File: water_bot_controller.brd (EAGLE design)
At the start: 100 x 80 mm, 55 parts

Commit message: added microcontroller module, cleaned up relay driver module
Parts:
- removed LED2, LED3, LED4: (no value), led:SMARTLED-TTW
- removed R10, R11, R12: 10k, rcl:R0603
- removed R7, R8, R9: 0 ohm, rcl:R0603
- added C1: 1uF, rcl:C0603
- added C2, C6: 0.1uF, rcl:C0603
- added C3, C5: 4.7uF, rcl:C1206
- added C4: 10uF, rcl:C1206
- added D1: MMBD4148DICT, LEDdynamics:SOT23
- added R22, R23: 10K, rcl:R0603
- added R24: 10 ohm, rcl:R0603
- added U$1: PSOC_4000, stovelite:SOIC16
- added U2: LM3480IM3-5.0, LEDdynamics:SOT-23
- IC1: value (none) -> ULN2803A
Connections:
- removed net 6C: IC1.13
- removed net 7C: IC1.12
- removed net 8C: IC1.11
- removed net N$10: IC1.7, R8.2
- removed net N$11: IC1.8, R9.2
- removed net N$12: IC1.2, R3.2
- removed net N$18: LED4.A@1, R12.1
- removed net N$19: LED3.A@1, R11.1
- removed net N$20: LED2.A@1, R10.1
- removed net N$9 (its old number): IC1.6, R7.2
- removed net P6: R12.2, R7.1
- removed net P7: R11.2, R8.1
- removed net P8: R10.2, R9.1
- new net N$37: C1.2, U$1.6
- new net N$38: D1.3, R24.1
- new net N$39: C4.1, R24.2, U2.2
- new net N$6: R3.2
- new net P0.2: R22.1, R23.2, U$1.4
- new net SCLK: U$1.2
- new net SDAT: U$1.1
- new net VDD: C2.1, C3.1, C5.1, C6.1, R22.2, U$1.7, U2.3
- net +12V: now also D1.1
- net GND: now also C1.1, C2.2, C3.2, C4.2, C5.2, C6.2, LED13.C@1, R23.1, U$1.8, U2.1; no longer LED2.C@1, LED3.C@1, LED4.C@1
- net N$35: now also R21.2
- net P1: now also U$1.16
- net P2: now also U$1.15
- net P3: now also U$1.14
- net P4: now also U$1.13
- net P5: now also U$1.12

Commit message: cleaned up relay module
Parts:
- removed LED11, LED12, LED13: (no value), led:SMARTLED-TTW
- removed R18, R19, R20, R21: 10K, rcl:R0603
- added LED2, LED3, LED4: (no value), led:SMARTLED-TTW
- added R10, R7, R8, R9: 10K, rcl:R0603
- moved LED10 519.6 mm to (-48.3, -709.9)
- moved RELAY_4 382.5 mm to (-73.7, -626.1)
- moved F4 354.5 mm to (-71.1, -647.7)
- moved F5 354.5 mm to (-71.1, -717.5)
- moved RELAY_5 354.5 mm to (-73.7, -696.0)
- moved TP7 354.5 mm to (-86.4, -664.2)
- moved TP8 354.5 mm to (-77.5, -664.2)
- moved TP10 354.5 mm to (-77.5, -734.1)
- moved TP9 354.5 mm to (-86.4, -734.1)
- moved TP5 315.6 mm to (-86.4, -594.4)
- moved TP6 315.6 mm to (-77.5, -594.4)
- moved F2 310.1 mm to (-71.1, -508.0)
- moved F3 310.1 mm to (-71.1, -577.9)
- moved RELAY_2 310.0 mm to (-73.7, -486.4)
- moved RELAY_3 310.0 mm to (-73.7, -556.3)
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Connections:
- net N$3 renamed R1
- removed net N$1 (its old number): RELAY_1.5, TP1.TP
- removed net N$21: RELAY_2.5, TP3.TP
- removed net N$23: F2.2, R18.2, TP4.TP
- removed net N$24: LED10.A@1, R18.1
- removed net N$25: RELAY_3.5, TP5.TP
- removed net N$27: F3.2, R19.2, TP6.TP
- removed net N$28: LED11.A@1, R19.1
- removed net N$29: RELAY_4.5, TP7.TP
- removed net N$31: F4.2, R20.2, TP8.TP
- removed net N$32: LED12.A@1, R20.1
- removed net N$33: RELAY_5.5, TP9.TP
- removed net N$35: F5.2, R21.2, TP10.TP
- removed net N$36: LED13.A@1, R21.1
- new net N$11: LED3.A@1, R8.1
- new net N$18: LED4.A@1, R9.1
- new net N$20: LED10.A@1, R10.1
- new net N$4: LED2.A@1, R7.1
- new net R2: F2.2, R7.2, TP4.TP
- new net R3: F3.2, R8.2, TP6.TP
- new net R4: F4.2, R9.2, TP8.TP
- new net R5: F5.2, R10.2, TP10.TP
- net 1C: now also RELAY_1.5, TP1.TP
- net 2C: now also RELAY_2.5, TP3.TP
- net 3C: now also RELAY_3.5, TP5.TP
- net 4C: now also RELAY_4.5, TP7.TP
- net 5C: now also RELAY_5.5, TP9.TP
- net GND: now also LED2.C@1, LED3.C@1, LED4.C@1; no longer LED11.C@1, LED12.C@1, LED13.C@1

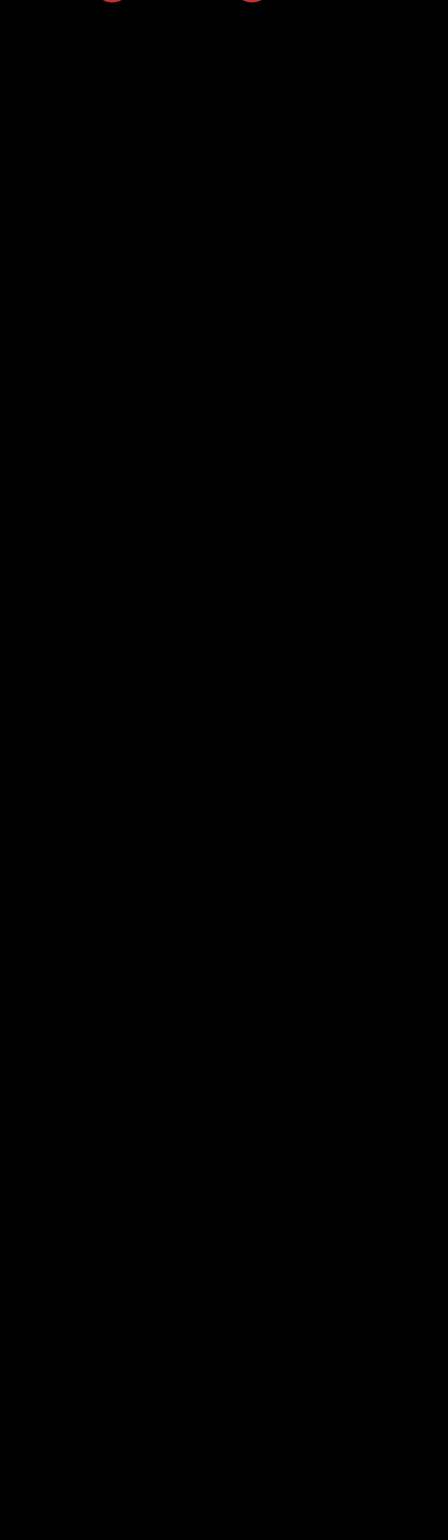
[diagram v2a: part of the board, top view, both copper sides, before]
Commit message: spec'd pwr/sig conns, added pushbuttons to schematic
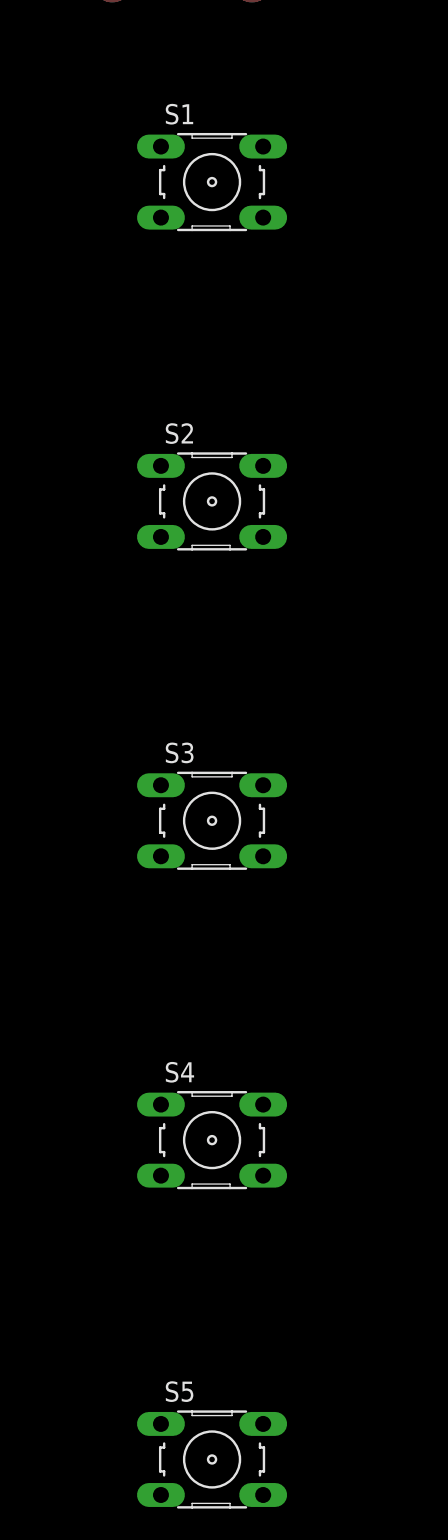
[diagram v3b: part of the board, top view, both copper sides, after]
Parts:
- added S1, S2, S3, S4, S5: (no value), switch-omron:B3F-10XX
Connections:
- net P1: now also S1.4
- net P2: now also S2.4
- net P3: now also S3.4
- net P4: now also S4.4
- net P5: now also S5.4
- net VDD: now also S1.2, S2.2, S3.2, S4.2, S5.2
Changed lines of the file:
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@@
 <element name="R10" library="rcl" library_urn="urn:adsk.eagle:library:334" package="R0603" package3d_urn="urn:adsk.eagle:package:23555/2" value="10K" x="-71.12" y="-732.79"/>
 <element name="LED10" library="led" library_urn="urn:adsk.eagle:library:259" package="SMARTLED-TTW" package3d_urn="urn:adsk.eagle:package:15825/1" value="" x="-48.26" y="-709.93"/>
+<element name="S1" library="switch-omron" library_urn="urn:adsk.eagle:library:377" package="B3F-10XX" package3d_urn="urn:adsk.eagle:package:27496/1" value="" x="-80.01" y="-746.76">
+<attribute name="MF" value="" x="-80.01" y="-746.76" size="1.778" layer="27" display="off"/>
+<attribute name="MPN" value="B3F-1000" x="-80.01" y="-746.76" size="1.778" layer="27" display="off"/>
+<attribute name="OC_FARNELL" value="176432" x="-80.01" y="-746.76" size="1.778" layer="27" display="off"/>
+<attribute name="OC_NEWARK" value="36M3542" x="-80.01" y="-746.76" size="1.778" layer="27" display="off"/>
+</element>
+<element name="S2" library="switch-omron" library_urn="urn:adsk.eagle:library:377" package="B3F-10XX" package3d_urn="urn:adsk.eagle:package:27496/1" value="" x="-80.01" y="-767.08">
+<attribute name="MF" value="" x="-80.01" y="-767.08" size="1.778" layer="27" display="off"/>
+<attribute name="MPN" value="B3F-1000" x="-80.01" y="-767.08" size="1.778" layer="27" display="off"/>
+<attribute name="OC_FARNELL" value="176432" x="-80.01" y="-767.08" size="1.778" layer="27" display="off"/>
+<attribute name="OC_NEWARK" value="36M3542" x="-80.01" y="-767.08" size="1.778" layer="27" display="off"/>
+</element>
+<element name="S3" library="switch-omron" library_urn="urn:adsk.eagle:library:377" package="B3F-10XX" package3d_urn="urn:adsk.eagle:package:27496/1" value="" x="-80.01" y="-787.4">
+<attribute name="MF" value="" x="-80.01" y="-787.4" size="1.778" layer="27" display="off"/>
+<attribute name="MPN" value="B3F-1000" x="-80.01" y="-787.4" size="1.778" layer="27" display="off"/>
+<attribute name="OC_FARNELL" value="176432" x="-80.01" y="-787.4" size="1.778" layer="27" display="off"/>
+<attribute name="OC_NEWARK" value="36M3542" x="-80.01" y="-787.4" size="1.778" layer="27" display="off"/>
+</element>
+<element name="S4" library="switch-omron" library_urn="urn:adsk.eagle:library:377" package="B3F-10XX" package3d_urn="urn:adsk.eagle:package:27496/1" value="" x="-80.01" y="-807.72">
+<attribute name="MF" value="" x="-80.01" y="-807.72" size="1.778" layer="27" display="off"/>
+<attribute name="MPN" value="B3F-1000" x="-80.01" y="-807.72" size="1.778" layer="27" display="off"/>
+<attribute name="OC_FARNELL" value="176432" x="-80.01" y="-807.72" size="1.778" layer="27" display="off"/>
+<attribute name="OC_NEWARK" value="36M3542" x="-80.01" y="-807.72" size="1.778" layer="27" display="off"/>
+</element>
+<element name="S5" library="switch-omron" library_urn="urn:adsk.eagle:library:377" package="B3F-10XX" package3d_urn="urn:adsk.eagle:package:27496/1" value="" x="-80.01" y="-828.04">
+<attribute name="MF" value="" x="-80.01" y="-828.04" size="1.778" layer="27" display="off"/>
+<attribute name="MPN" value="B3F-1000" x="-80.01" y="-828.04" size="1.778" layer="27" display="off"/>
+<attribute name="OC_FARNELL" value="176432" x="-80.01" y="-828.04" size="1.778" layer="27" display="off"/>
+<attribute name="OC_NEWARK" value="36M3542" x="-80.01" y="-828.04" size="1.778" layer="27" display="off"/>
+</element>
 </elements>
 <signals>
@@
 <contactref element="R6" pad="1"/>
 <contactref element="R13" pad="2"/>
+<contactref element="S5" pad="4"/>
 <wire x1="-37.25" y1="-124.46" x2="-86.995" y2="-378.52" width="0" layer="19" extent="1-1"/>
 <wire x1="-38.95" y1="-88.9" x2="-37.25" y2="-124.46" width="0" layer="19" extent="1-1"/>
+<wire x1="-76.7588" y1="-830.3006" x2="-86.995" y2="-378.52" width="0" layer="19" extent="1-1"/>
 </signal>
 <signal name="P4">
@@
 <contactref element="R14" pad="2"/>
 <contactref element="R5" pad="1"/>
+<contactref element="S4" pad="4"/>
 <wire x1="-37.25" y1="-129.54" x2="-85.725" y2="-378.52" width="0" layer="19" extent="1-1"/>
 <wire x1="-38.95" y1="-83.82" x2="-37.25" y2="-129.54" width="0" layer="19" extent="1-1"/>
+<wire x1="-76.7588" y1="-809.9806" x2="-85.725" y2="-378.52" width="0" layer="19" extent="1-1"/>
 </signal>
 <signal name="P3">
@@
 <contactref element="R4" pad="1"/>
 <contactref element="R15" pad="2"/>
+<contactref element="S3" pad="4"/>
 <wire x1="-37.25" y1="-134.62" x2="-84.455" y2="-378.52" width="0" layer="19" extent="1-1"/>
 <wire x1="-38.95" y1="-78.74" x2="-37.25" y2="-134.62" width="0" layer="19" extent="1-1"/>
+<wire x1="-76.7588" y1="-789.6606" x2="-84.455" y2="-378.52" width="0" layer="19" extent="1-1"/>
 </signal>
 <signal name="P2">
@@
 <contactref element="R3" pad="1"/>
 <contactref element="R16" pad="2"/>
+<contactref element="S2" pad="4"/>
 <wire x1="-37.25" y1="-139.7" x2="-83.185" y2="-378.52" width="0" layer="19" extent="1-1"/>
 <wire x1="-38.95" y1="-73.66" x2="-37.25" y2="-139.7" width="0" layer="19" extent="1-1"/>
+<wire x1="-76.7588" y1="-769.3406" x2="-83.185" y2="-378.52" width="0" layer="19" extent="1-1"/>
 </signal>
 <signal name="P1">
@@
 <contactref element="R2" pad="1"/>
 <contactref element="R17" pad="2"/>
+<contactref element="S1" pad="4"/>
 <wire x1="-37.25" y1="-144.78" x2="-81.915" y2="-378.52" width="0" layer="19" extent="1-1"/>
 <wire x1="-38.95" y1="-68.58" x2="-37.25" y2="-144.78" width="0" layer="19" extent="1-1"/>
+<wire x1="-76.7588" y1="-749.0206" x2="-81.915" y2="-378.52" width="0" layer="19" extent="1-1"/>
 </signal>
 <signal name="N$13">
@@
 <contactref element="C5" pad="1"/>
 <contactref element="C6" pad="1"/>
+<contactref element="S1" pad="2"/>
+<contactref element="S2" pad="2"/>
+<contactref element="S3" pad="2"/>
+<contactref element="S4" pad="2"/>
+<contactref element="S5" pad="2"/>
 <wire x1="-90.3" y1="-421.64" x2="-87.9094" y2="-414.274" width="0" layer="19" extent="1-1"/>
 <wire x1="-88.05" y1="-402.59" x2="-87.9094" y2="-414.274" width="0" layer="19" extent="1-1"/>
@@
 <wire x1="-90.3" y1="-448.31" x2="-90.3" y2="-421.64" width="0" layer="19" extent="1-1"/>
 <wire x1="-88.48" y1="-454.66" x2="-90.3" y2="-448.31" width="0" layer="19" extent="1-1"/>
+<wire x1="-76.7588" y1="-744.4994" x2="-88.48" y2="-454.66" width="0" layer="19" extent="1-1"/>
+<wire x1="-76.7588" y1="-764.8194" x2="-76.7588" y2="-744.4994" width="0" layer="19" extent="1-1"/>
+<wire x1="-76.7588" y1="-785.1394" x2="-76.7588" y2="-764.8194" width="0" layer="19" extent="1-1"/>
+<wire x1="-76.7588" y1="-805.4594" x2="-76.7588" y2="-785.1394" width="0" layer="19" extent="1-1"/>
+<wire x1="-76.7588" y1="-825.7794" x2="-76.7588" y2="-805.4594" width="0" layer="19" extent="1-1"/>
 </signal>
 <signal name="P0.2">

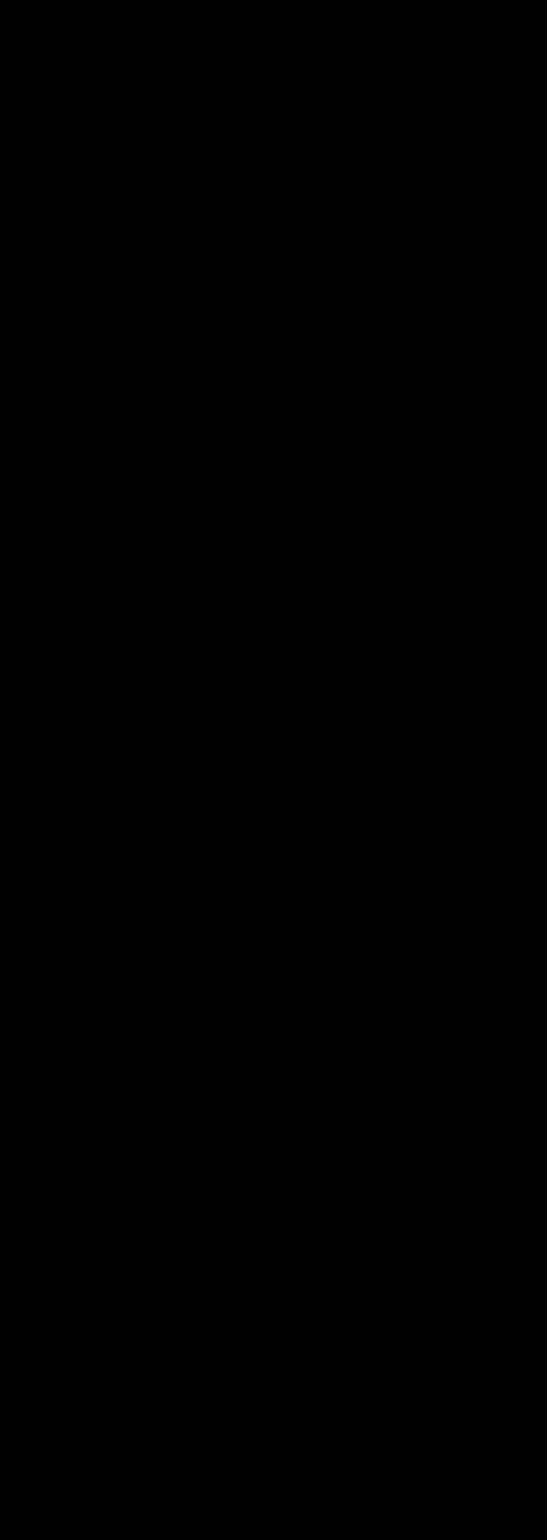
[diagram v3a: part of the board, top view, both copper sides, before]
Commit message: added optional particle photon headers
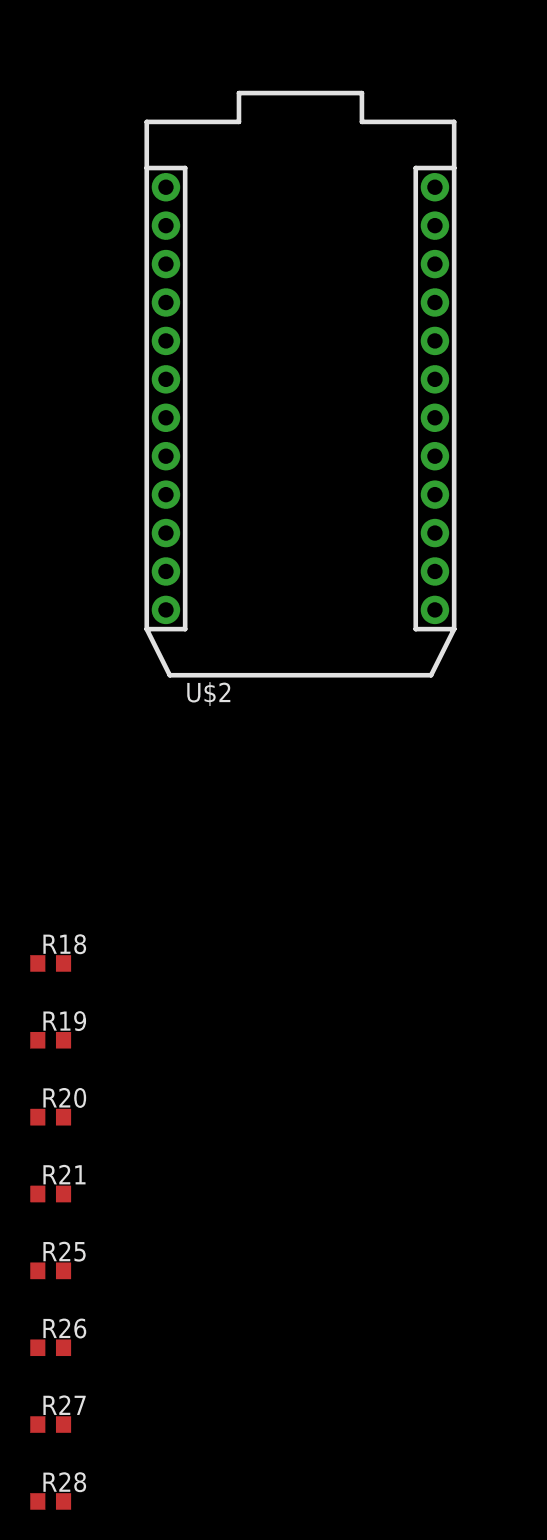
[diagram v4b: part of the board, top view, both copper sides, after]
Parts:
- added R18, R19, R20, R21, R25, R26, R27, R28: 0 ohm, rcl:R0603
- added U$2: PHOTON_WITH_HEADERS, Spark:PHOTON
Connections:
- removed net SCLK: U$1.2
- removed net SDAT: U$1.1
- new net N$21: R26.1, U$2.15
- new net N$22: R27.1, U$2.14
- new net N$23: R18.1, U$2.24
- new net N$24: R19.1, U$2.19
- new net N$25: R20.1, U$2.18
- new net N$26: R21.1, U$2.17
- new net N$27: R25.1, U$2.16
- new net N$28: R28.1, U$2.13
- new net SCL: R27.2, U$1.2
- new net SDA: R28.2, U$1.1
- new net VBAT: U$2.22
- new net VIN: U$2.1
- net GND: now also U$2.2, U$2.21
- net P1: now also R19.2
- net P2: now also R20.2
- net P3: now also R21.2
- net P4: now also R25.2
- net P5: now also R26.2
- net VDD: now also R18.2

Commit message: added i2c isolation circuitry, replaced leds, and added test points
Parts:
- removed D1: MMBD4148DICT, LEDdynamics:SOT23
- removed R22, R23: 10K, rcl:R0603
- added +12V, GND, I2C_3V3, I2C_GND, I2C_SCL, I2C_SDA, RELAY1, RELAY2, RELAY3, RELAY4, RELAY5, RELAY_GND: WIREPAD3,17/1,3, wirepad:3,17/1,3
- added C10: 4.7uF, rcl:C1206
- added C7, C8: 10uF, rcl:C1206
- added C9: 0.1uF, rcl:C0603
- added R11, R12, R29, R30: 1K, rcl:R0603
- added TP11, TP12, TP13, TP14, TP15, TP16, TP17, TP18, TP19, TP20, TP21, TP22, TP23: PTR1B2,54, testpad:B2,54
- added U$3: ISO1540, ISO1540:SOIC8
- LED1, LED10, LED2, LED3, LED4, LED5, LED6, LED7, LED8: device led:SMARTLED-TTW -> led:CHIP-LED0603
- moved LED1 1033.1 mm to (-146.1, -1068.1)
- moved LED5 930.2 mm to (-171.4, -1068.1)
- moved LED6 930.2 mm to (-176.5, -1068.1)
- moved LED7 930.2 mm to (-181.6, -1068.1)
- moved LED8 930.2 mm to (-186.7, -1068.1)
- moved LED2 578.2 mm to (-151.1, -1068.1)
- moved LED3 510.7 mm to (-156.2, -1068.1)
- moved LED4 443.9 mm to (-161.3, -1068.1)
- moved LED10 377.1 mm to (-166.4, -1068.1)
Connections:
- removed net GND: C1.1, C2.2, C3.2, C4.2, C5.2, C6.2, IC1.9, LED1.C@1, LED10.C@1, LED2.C@1, LED3.C@1, LED4.C@1, LED5.C@1, LED6.C@1, LED7.C@1, LED8.C@1, LED9.C@1, R23.1, U$1.8, U$2.2, U$2.21, U2.1
- removed net N$37: C1.2, U$1.6
- removed net N$38: D1.3, R24.1
- removed net P0.2: R22.1, R23.2, U$1.4
- removed net VDD: C2.1, C3.1, C5.1, C6.1, R18.2, R22.2, S1.2, S2.2, S3.2, S4.2, S5.2, U$1.7, U2.3
- new net +3V3: C2.1, C3.1, C5.1, C6.1, C8.1, R18.2, R29.2, R30.2, S1.2, S2.2, S3.2, S4.2, S5.2, TP11.TP, U$1.7, U$3.8, U2.3
- new net 12V_IN: +12V.1, TP21.TP
- new net GND1: C7.2, GND.1, I2C_GND.1, IC1.9, LED1.C, LED10.C, LED2.C, LED3.C, LED4.C, LED5.C, LED6.C, LED7.C, LED8.C, LED9.C@1, RELAY_GND.1, TP17.TP, TP18.TP, TP20.TP, U$3.4
- new net GND2: C1.2, C10.2, C2.2, C3.2, C4.2, C5.2, C6.2, C8.2, C9.2, U$1.8, U$2.2, U$2.21, U$3.5, U2.1
- new net I2C_3V3: C7.1, I2C_3V3.1, R11.2, R12.2, TP23.TP, U$3.1
- new net I2C_SCL: I2C_SCL.1, R12.1, TP19.TP, U$3.3
- new net I2C_SDA: I2C_SDA.1, R11.1, TP22.TP, U$3.2
- new net N$29: C1.1, U$1.6
- net +12V: now also R24.1; no longer D1.1
- net N$1: now also LED1.A; no longer LED1.A@1
- net N$11: now also LED3.A; no longer LED3.A@1
- net N$14: now also LED5.A; no longer LED8.A@1
- net N$15: now also LED6.A; no longer LED7.A@1
- net N$16: now also LED7.A; no longer LED6.A@1
- net N$17: now also LED8.A; no longer LED5.A@1
- net N$18: now also LED4.A; no longer LED4.A@1
- net N$20: now also LED10.A; no longer LED10.A@1
- net N$23: now also C10.1, C9.1
- net N$4: now also LED2.A; no longer LED2.A@1
- net R1: now also RELAY1.1, TP12.TP
- net R2: now also RELAY2.1, TP13.TP
- net R3: now also RELAY3.1, TP14.TP
- net R4: now also RELAY4.1, TP15.TP
- net R5: now also RELAY5.1, TP16.TP
- net SCL: now also R30.1, U$3.6
- net SDA: now also R29.1, U$3.7
